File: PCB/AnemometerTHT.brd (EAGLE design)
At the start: 150 x 100 mm, 39 parts, among them IC1 TINY2313A, IC2 74HC151D, IC3 74HC151D, IC4 74HC08D, IC5 LM555N, IC6 74HC138D, IC7 74CH14D, IC8 74HC393D, Q1 16MHz

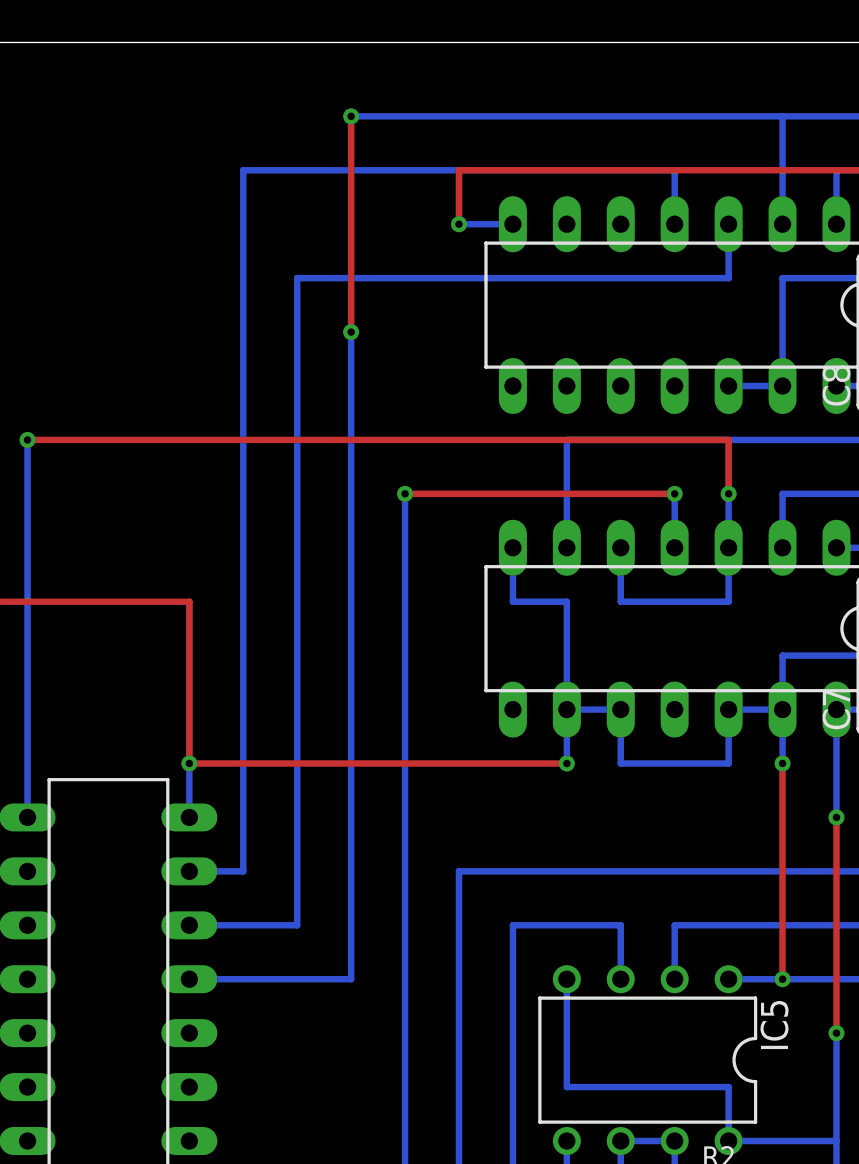
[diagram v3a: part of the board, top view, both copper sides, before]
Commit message: moved puls counter to in/4
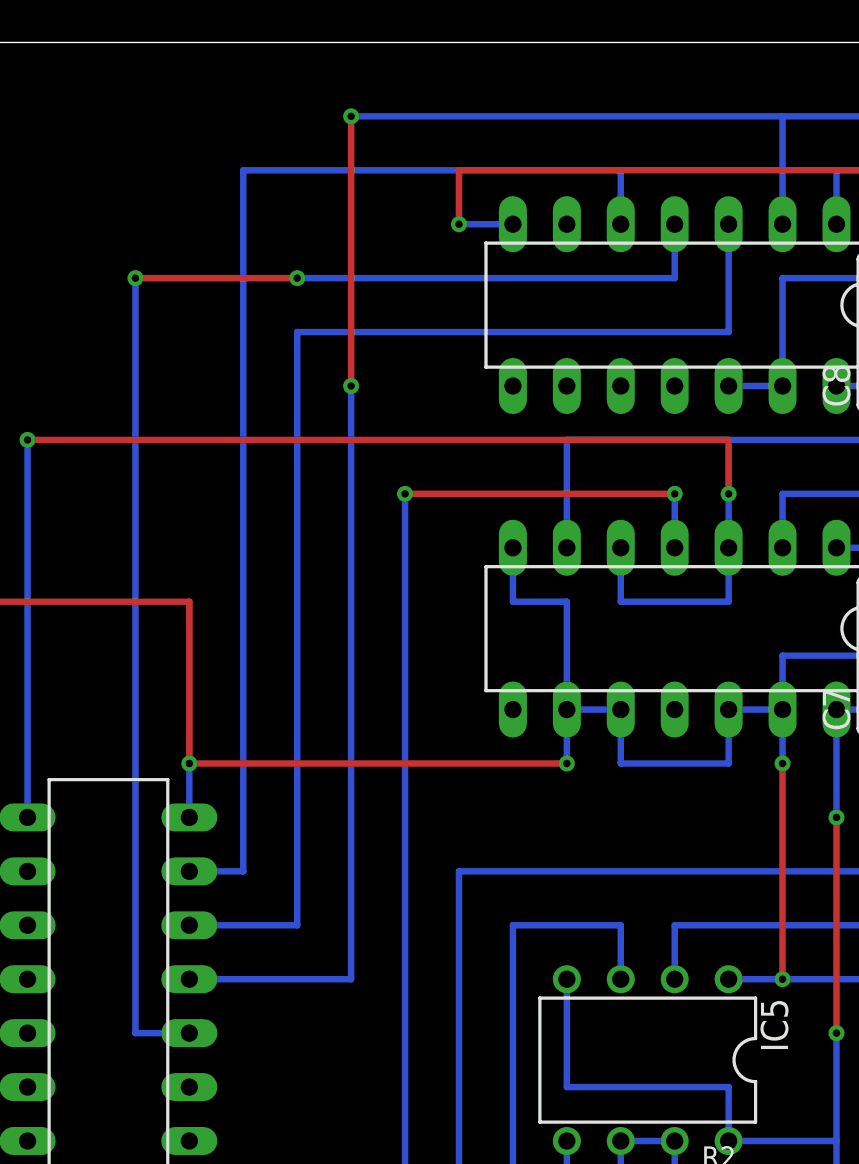
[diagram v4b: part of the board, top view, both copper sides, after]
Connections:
- new net PULS*4: IC1.8, IC8.3
- net PULS: now also IC8.5; no longer IC8.4
- net PULS*2: now also IC1.6, IC8.4; no longer IC1.8, IC8.3
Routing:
- net PULS*4: track 0.00 -> 58.4 mm
- net PULS*2: track 58.4 -> 66.0 mm, vias 0 -> 2
- net PULS: track 58.4 -> 55.9 mm
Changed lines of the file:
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@@
 <contactref element="IC8" pad="2"/>
 <wire x1="30.48" y1="55.88" x2="38.1" y2="55.88" width="0.3048" layer="16"/>
-<wire x1="38.1" y1="55.88" x2="38.1" y2="86.36" width="0.3048" layer="16"/>
-<via x="38.1" y="86.36" extent="1-16" drill="0.35"/>
-<wire x1="38.1" y1="86.36" x2="38.1" y2="96.52" width="0.3048" layer="1"/>
+<wire x1="38.1" y1="55.88" x2="38.1" y2="83.82" width="0.3048" layer="16"/>
+<via x="38.1" y="83.82" extent="1-16" drill="0.35"/>
+<wire x1="38.1" y1="83.82" x2="38.1" y2="96.52" width="0.3048" layer="1"/>
 <via x="38.1" y="96.52" extent="1-16" drill="0.35"/>
 <wire x1="38.1" y1="96.52" x2="58.42" y2="96.52" width="0.3048" layer="16"/>
@@
 <signal name="PULS">
 <contactref element="IC1" pad="9"/>
-<contactref element="IC8" pad="4"/>
 <wire x1="30.48" y1="60.96" x2="33.02" y2="60.96" width="0.3048" layer="16"/>
-<wire x1="33.02" y1="93.98" x2="53.34" y2="93.98" width="0.3048" layer="16"/>
-<wire x1="53.34" y1="93.98" x2="53.34" y2="91.44" width="0.3048" layer="16"/>
+<wire x1="33.02" y1="93.98" x2="50.8" y2="93.98" width="0.3048" layer="16"/>
 <wire x1="33.02" y1="60.96" x2="33.02" y2="93.98" width="0.3048" layer="16"/>
+<contactref element="IC8" pad="5"/>
+<wire x1="50.8" y1="91.44" x2="50.8" y2="93.98" width="0.3048" layer="16"/>
 </signal>
 <signal name="TIME">
@@
 </signal>
 <signal name="PULS*2">
-<contactref element="IC1" pad="8"/>
-<contactref element="IC8" pad="3"/>
-<wire x1="35.56" y1="58.42" x2="30.48" y2="58.42" width="0.3048" layer="16"/>
-<wire x1="55.88" y1="91.44" x2="55.88" y2="88.9" width="0.3048" layer="16"/>
-<wire x1="55.88" y1="88.9" x2="35.56" y2="88.9" width="0.3048" layer="16"/>
-<wire x1="35.56" y1="88.9" x2="35.56" y2="58.42" width="0.3048" layer="16"/>
+<contactref element="IC8" pad="4"/>
+<contactref element="IC1" pad="6"/>
+<wire x1="30.48" y1="53.34" x2="27.94" y2="53.34" width="0.3048" layer="16"/>
+<wire x1="27.94" y1="53.34" x2="27.94" y2="88.9" width="0.3048" layer="16"/>
+<wire x1="53.34" y1="91.44" x2="53.34" y2="88.9" width="0.3048" layer="16"/>
+<wire x1="53.34" y1="88.9" x2="35.56" y2="88.9" width="0.3048" layer="16"/>
+<via x="35.56" y="88.9" extent="1-16" drill="0.35"/>
+<wire x1="35.56" y1="88.9" x2="27.94" y2="88.9" width="0.3048" layer="1"/>
+<via x="27.94" y="88.9" extent="1-16" drill="0.35"/>
 </signal>
 <signal name="A">
@@
 <wire x1="10.16" y1="45.72" x2="10.16" y2="50.8" width="0.3048" layer="16"/>
 </signal>
+<signal name="PULS*4">
+<contactref element="IC8" pad="3"/>
+<contactref element="IC1" pad="8"/>
+<wire x1="35.56" y1="58.42" x2="30.48" y2="58.42" width="0.3048" layer="16"/>
+<wire x1="55.88" y1="86.36" x2="35.56" y2="86.36" width="0.3048" layer="16"/>
+<wire x1="35.56" y1="86.36" x2="35.56" y2="58.42" width="0.3048" layer="16"/>
+<wire x1="55.88" y1="91.44" x2="55.88" y2="86.36" width="0.3048" layer="16"/>
+</signal>
 </signals>
